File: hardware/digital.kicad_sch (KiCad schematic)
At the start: 18 parts, among them J1 IPEX-1, J2 IPEX-1, J3 IPEX-1, J4 IPEX-1, J5 IPEX-1, J6 IPEX-1, J7 IPEX-1, J8 IPEX-1, J9 IPEX-1

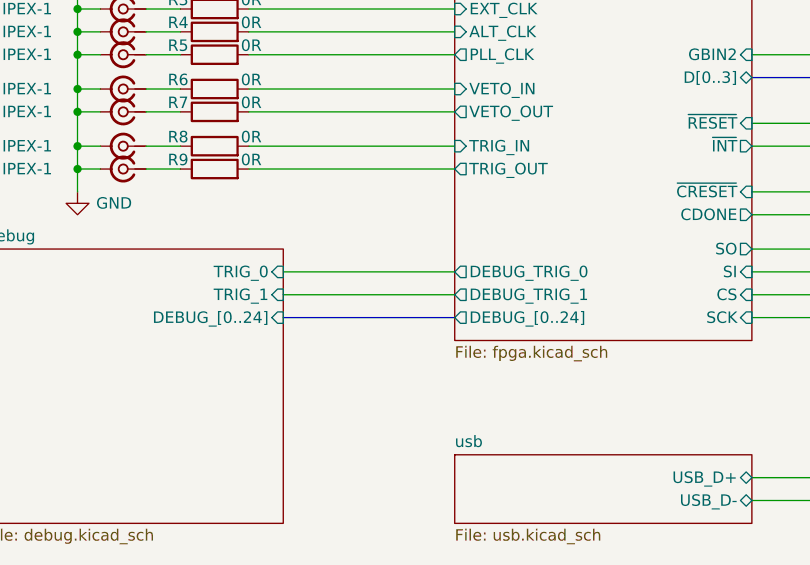
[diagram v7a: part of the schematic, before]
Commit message: route all signal
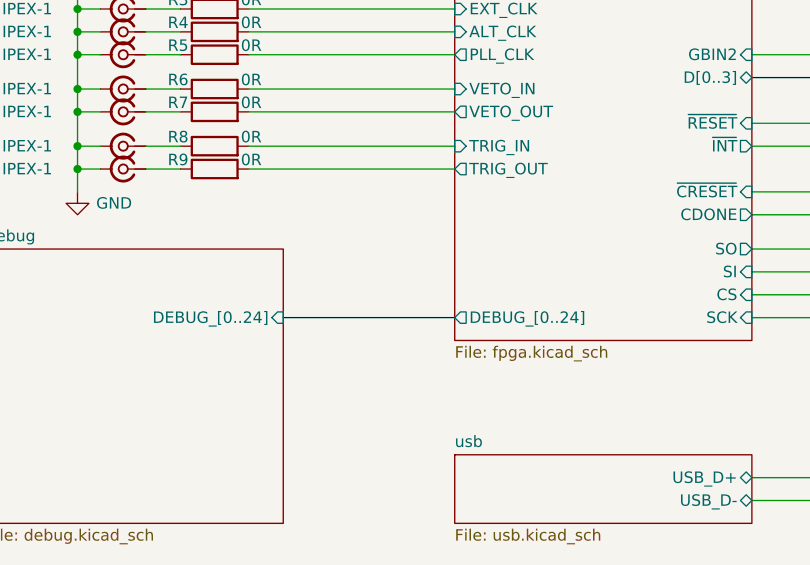
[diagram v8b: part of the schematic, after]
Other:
- sheet FPGA ports: added none; removed DEBUG_TRIG_0, DEBUG_TRIG_1
- sheet debug ports: added none; removed TRIG_0, TRIG_1
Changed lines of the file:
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@@
-	(wire
-		(pts
-			(xy 111.76 128.27) (xy 130.81 128.27)
-		)
-		(stroke
-			(width 0)
-			(type default)
-		)
-	)
 	(wire
 		(pts
@@
 		(pts
 			(xy 88.9 101.6) (xy 91.44 101.6)
-		)
-		(stroke
-			(width 0)
-			(type default)
-		)
-	)
-	(wire
-		(pts
-			(xy 111.76 125.73) (xy 130.81 125.73)
 		)
 		(stroke
@@
 			)
 		)
-		(pin "DEBUG_TRIG_1" output
-			(at 130.81 128.27 180)
-			(effects
-				(font
-					(size 1.27 1.27)
-				)
-				(justify left)
-			)
-		)
-		(pin "DEBUG_TRIG_0" output
-			(at 130.81 125.73 180)
-			(effects
-				(font
-					(size 1.27 1.27)
-				)
-				(justify left)
-			)
-		)
 		(pin "BNC_[0..1]" bidirectional
 			(at 130.81 86.36 180)
@@
 			)
 		)
-		(pin "TRIG_0" input
-			(at 111.76 125.73 0)
-			(effects
-				(font
-					(size 1.27 1.27)
-				)
-				(justify right)
-			)
-		)
-		(pin "TRIG_1" input
-			(at 111.76 128.27 0)
-			(effects
-				(font
-					(size 1.27 1.27)
-				)
-				(justify right)
-			)
-		)
